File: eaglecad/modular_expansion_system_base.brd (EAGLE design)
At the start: 90.2 x 100 mm, 40 parts, among them IC1 74LS244N, IC10 74LS30N, IC2 74LS244N, IC3 74LS244N, IC4 SRAM, IC5 74LS30N, IC6 LM2596T-5.0, IC8 74LS00N, IC9 7805T, J1-INTERRUPTS INTERRUPTS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

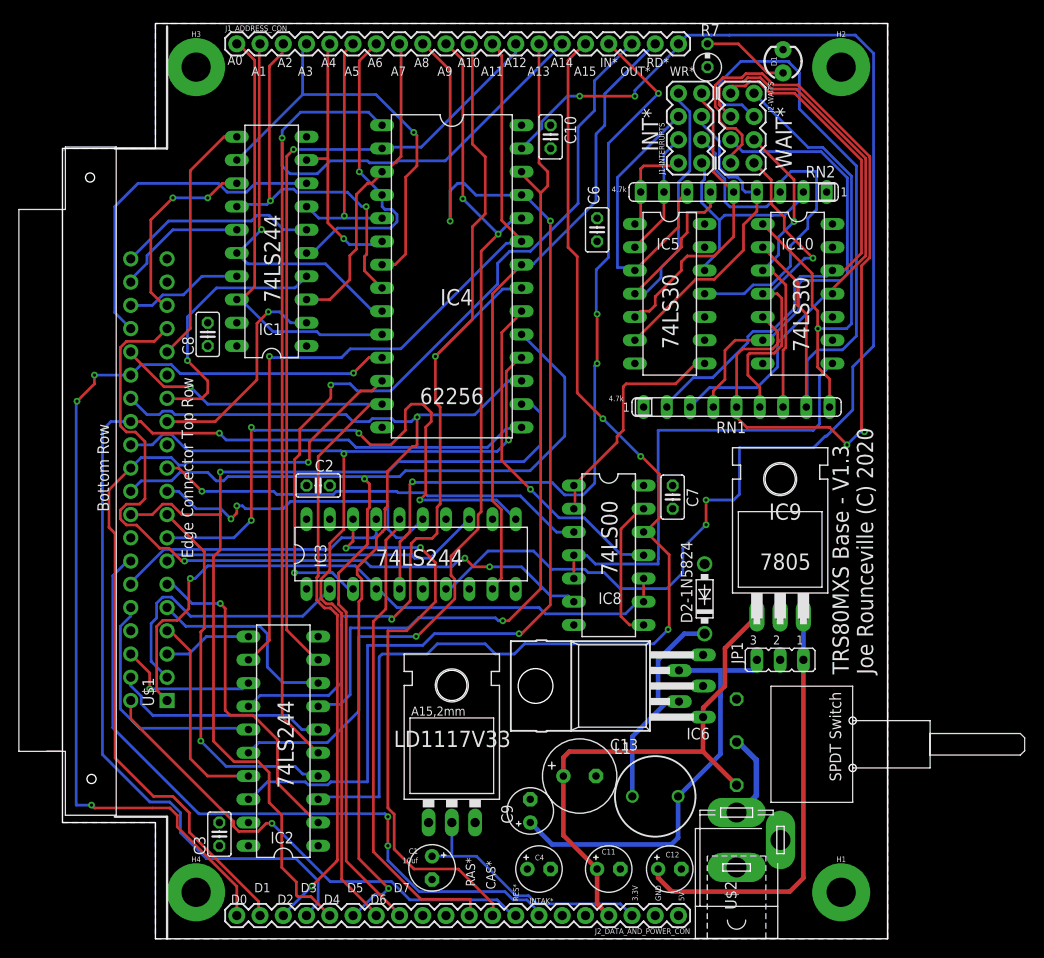
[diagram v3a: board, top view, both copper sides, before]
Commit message: Fixes for mount, stand alond joystick boards, level shifters Adafruit
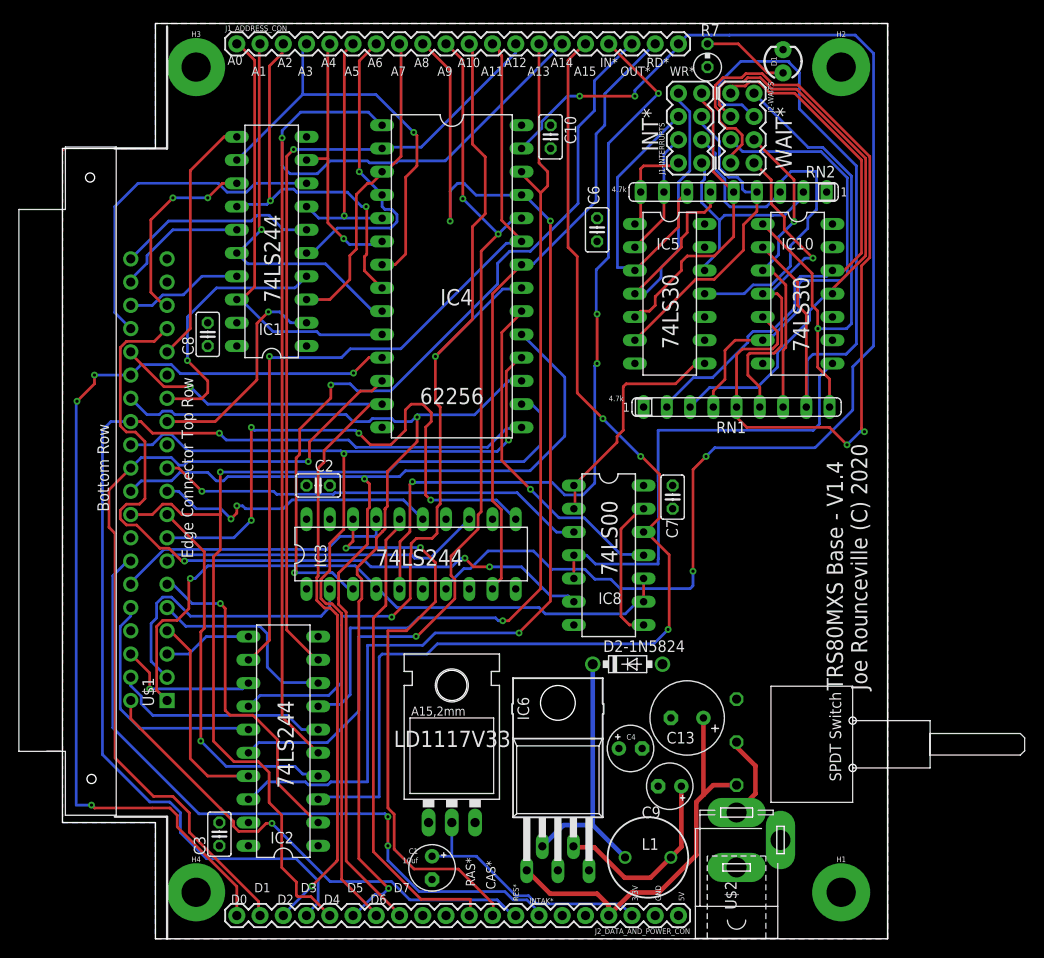
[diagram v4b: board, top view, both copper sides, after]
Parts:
- removed C11: 100uf, rcl:E2,5-5
- removed C12: 10uf, resistor:E2,5-5
- removed IC9: 7805T, linear:TO220H
- removed JP1: 5V_SOURCE, jumper:JP2
- moved C4 16.5 mm to (62.1, 20.8)
- moved C9 15.5 mm to (66.4, 16.7), turned to 180 degrees
- moved C13 13.4 mm to (68.3, 24.1), turned to 180 degrees
- moved D2-1N5824 11.0 mm to (61.8, 30.0), turned to 0 degrees
- moved L1 6.71 mm to (64.0, 8.89)
- moved IC6 5.32 mm to (54.1, 28.6), turned to 0 degrees
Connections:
- removed net 5V_FROM_LINEAR_REG: C12.+, IC9.3, JP1.1
- net 5V_FROM_SWITCHER: no longer JP1.3
- net 9V-POST-SW: no longer C11.+, IC9.1
- net GND: no longer C11.-, C12.-, IC9.2
- net VCC: no longer JP1.2
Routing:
- net 5V_FROM_LINEAR_REG: track 46.7 -> 0.00 mm
- net 5V_FROM_SWITCHER: track 47.2 -> 21.2 mm
- net 9V-POST-SW: track 57.3 -> 43.3 mm
- net IN*: track 35.0 -> 31.7 mm
- net N$1: track 26.3 -> 29.0 mm
- net BUFFERED_WR*: track 147.4 -> 148.9 mm
- net RD*: track 65.5 -> 64.3 mm
- net CAS*: track 30.4 -> 31.5 mm
- net BUFFERED_A15: track 127.6 -> 126.7 mm
- net WAIT2*: track 79.5 -> 80.0 mm
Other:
- board text added: "TRS80MXS Base - V1.4 Joe Rounceville (C) 2020"
- board text removed: "7805"
- board text removed: "TRS80MXS Base - V1.3 Joe Rounceville (C) 2020"
